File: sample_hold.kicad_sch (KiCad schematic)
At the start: 40 parts, among them K21 G6K-2FY, 5V, Q201 AO3400A, Q202 AO3401A, Q203 AO3400A, Q204 AO3400A, Q205 AO3400A, Q206 AO3400A, Q207 AO3400A, U19 TCA0372, U21 OPA828DGN, U22 OPA2197D

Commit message: Progress checkin.  About to redo FDA feedback again.
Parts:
- removed U19: TCA0372, Package_SO:SOIC-16W_7.5x10.3mm_P1.27mm, symbol Parts:TCA0372
- added C203, C205: 10u, Capacitor_SMD:C_0805_2012Metric, symbol Device:C
- added C210: 0u1, Capacitor_SMD:C_0402_1005Metric, symbol Device:C
- added unit 2 of K21
- added unit 3 of K21
- added R266: 200k, Resistor_SMD:R_0402_1005Metric, symbol Device:R
- added U23: TLV9352D, Parts:TLV9352D, symbol Parts:TLV9352D
- C201: footprint Parts:C_Rect_L31.5mm_W15.0mm_P27.50mm_MKS4 -> Parts:C_Rect_L31.5mm_W15.0mm_P27.50mm_Duo
- C204: value 10n -> 0u1; footprint Capacitor_SMD:C_0603_1608Metric -> Capacitor_SMD:C_0402_1005Metric; LCSC C307500 -> C307331
- K21: footprint Relay_SMD:Relay_DPDT_Omron_G6K-2G-Y -> Relay_SMD:Relay_DPDT_Omron_G6K-2F-Y; symbol Relay:G6K-2 -> Parts:G6K_Split
- R202: value 100k -> 200k; LCSC C25741 -> (none)
- R214: footprint Resistor_SMD:R_0402_1005Metric -> Resistor_SMD:R_0603_1608Metric; LCSC C25087 -> (none)
- U21: footprint Parts:VSSOP-8-1EP_3x3mm_P0.65mm_EP1.57x1.89mm -> Parts:OPA828DGN_guard
- renumbered C205 to C21, Q201 to Q21, Q202 to Q22, Q203 to Q23, Q205 to Q24, Q204 to Q25, Q206 to Q26, Q207 to Q27
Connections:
- net -18V: now also C205.2, C210.2, U23.4 (V-); no longer C207.2, C209.2, U21.4 (V-), U22.4 (V-)
- net DACref: now also U22.5 (+); no longer U22.3 (+)
- net Drive: now also K21.2, K21.3, K21.4, K21.6; no longer K21.3, K21.6
- net GND: now also Q27.3 (D), U22.3 (+); no longer C204.2, Q27.2 (S), U22.5 (+)
- net GNDPWR: now also C204.2, C203.2, C205.1, C210.1
- net SH: now also K21.5; no longer K21.4, K21.5
- net SHGnd: no longer C204.1
- net at R201.1, R202.2: now also C202.2, U22.6 (-), R266.2; no longer C202.1, U22.2 (-)
- net at R202.1, R205.1, R206.1: now also U23.6 (-), U23.7; no longer R203.1, R204.1
- net GComp: now reaches R213.2, R214.1
- net GComp: now also U22.1; no longer U22.7
- net at JP1.2 (B), Q26.3 (D): now also Q27.2 (S); no longer Q27.3 (D)
- net at R212.2, R213.1: now also U22.2 (-); no longer U22.6 (-)
- new net: R203.1, R204.1, R266.1, U23.1, U23.2 (-)
- new net: K21.7, R207.2
- new net +21V: C203.1, C204.1, U23.8 (V+)
- new net -16V: C207.2, C209.2, U21.4 (V-), U22.4 (V-)
- new net DACinner: C202.1, U22.7, U23.3 (+), U23.5 (+)
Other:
- moved on the sheet: C201, C202, C206, C207, C208, C209, C21, D22, JP1, Q24, Q25, Q26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

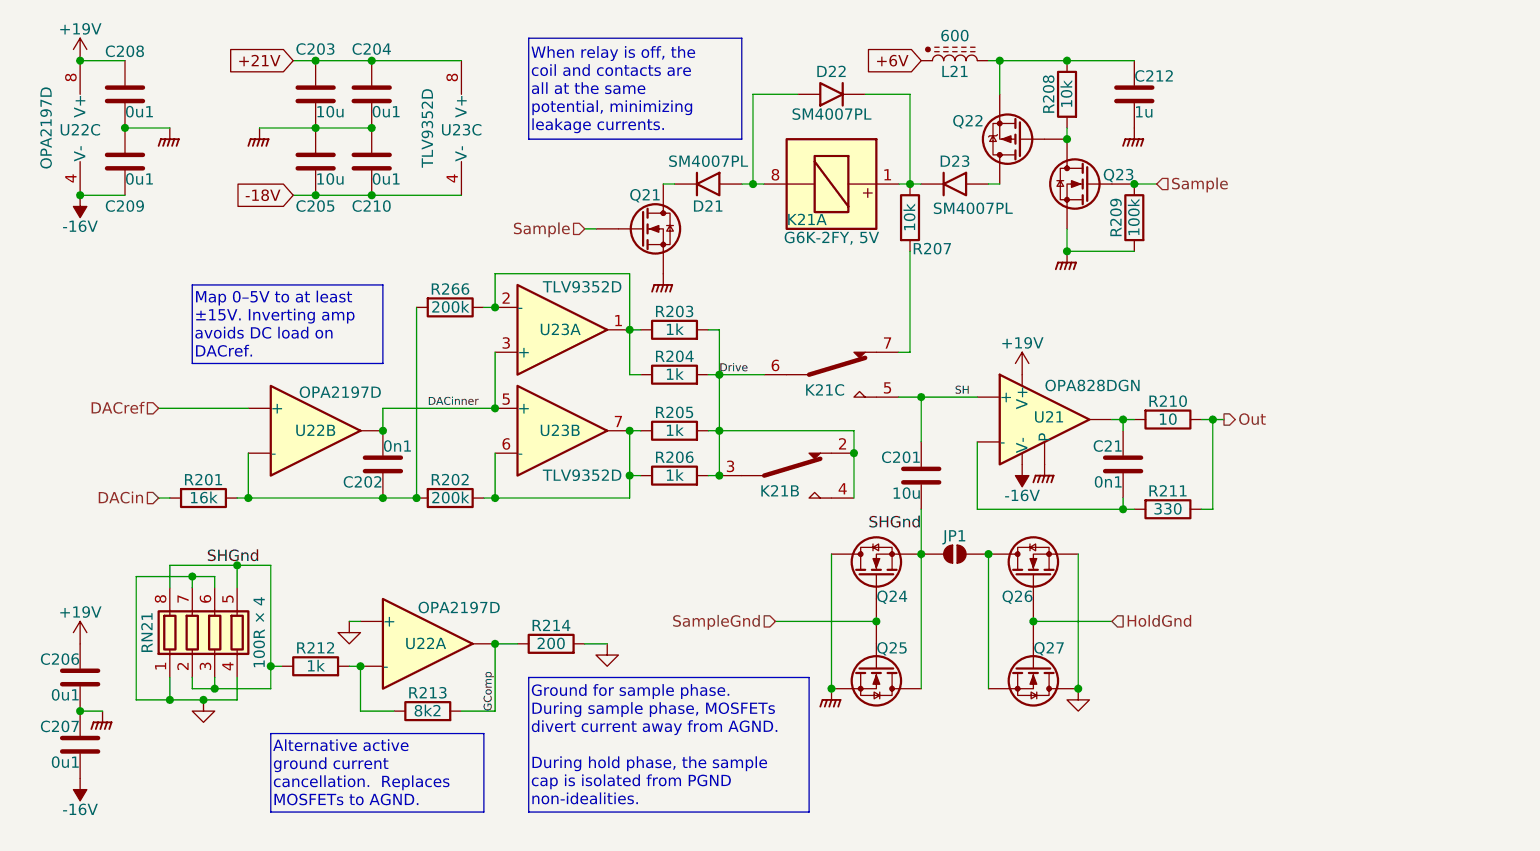
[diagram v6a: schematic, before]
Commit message: Start to place within physical board size.
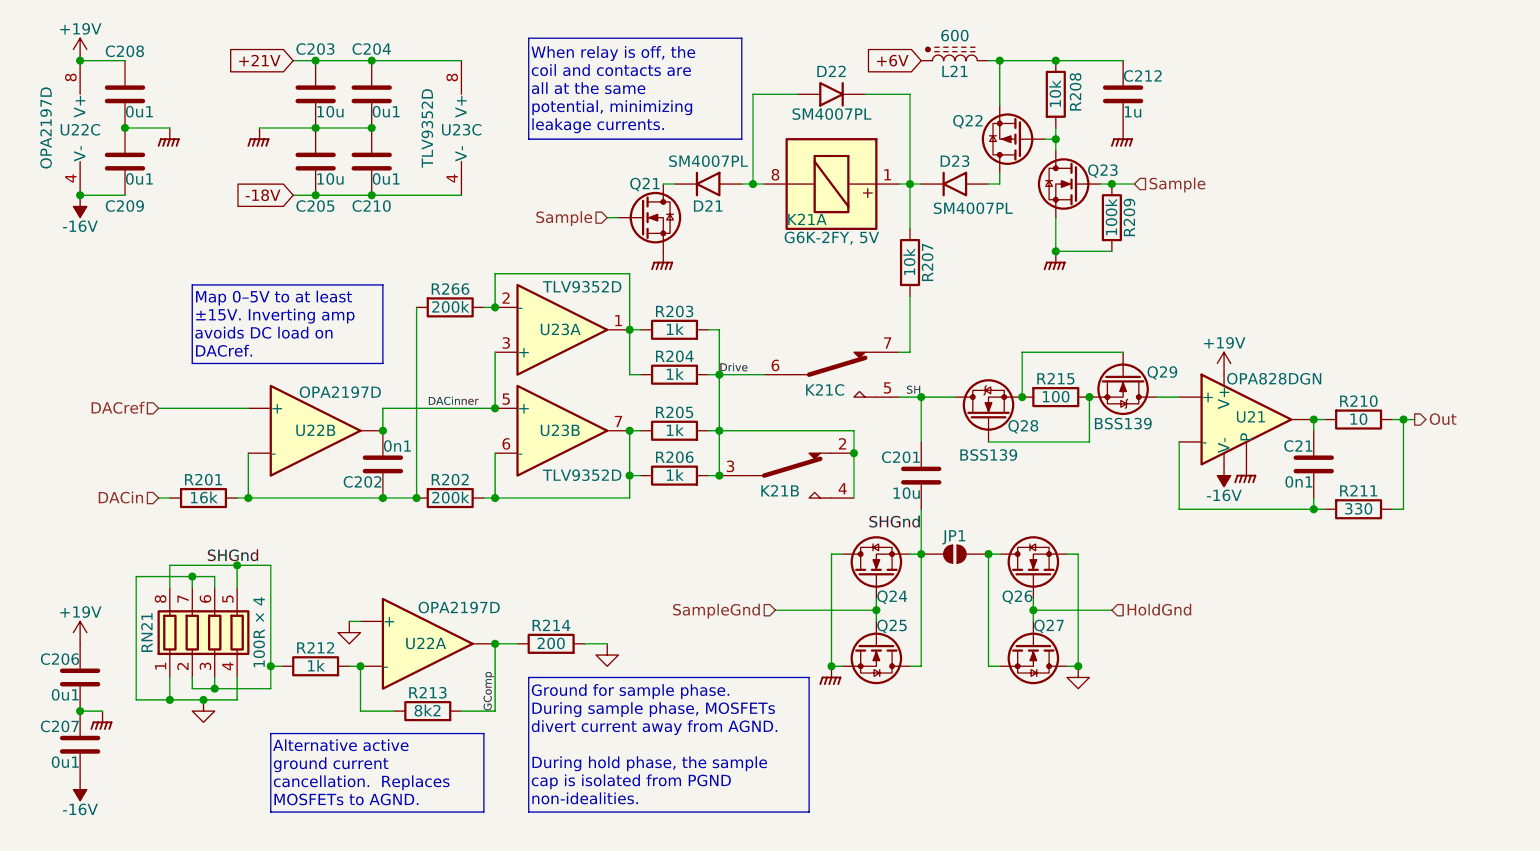
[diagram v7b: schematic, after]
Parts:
- added Q28, Q29: BSS139, Parts:SOT-23, symbol Parts:BSS139
- added R215: 100, Resistor_SMD:R_0402_1005Metric, symbol Device:R
- Q21, Q23, Q24, Q25, Q26, Q27: symbol Transistor_FET:AO3400A -> Parts:AO3400A; LCSC C20917 -> C15127
- Q22: symbol Transistor_FET:AO3401A -> Parts:AO3401A
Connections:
- net SH: now also Q28.3 (D); no longer U21.3 (+)
- new net: Q28.1 (G), Q29.2 (S), R215.1
- new net: Q28.2 (S), Q29.1 (G), R215.2
- new net: Q29.3 (D), U21.3 (+)
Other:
- moved on the sheet: C21, C212, Q21, Q22, Q23, Q24, Q25, Q26, Q27, R207, R208, R209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

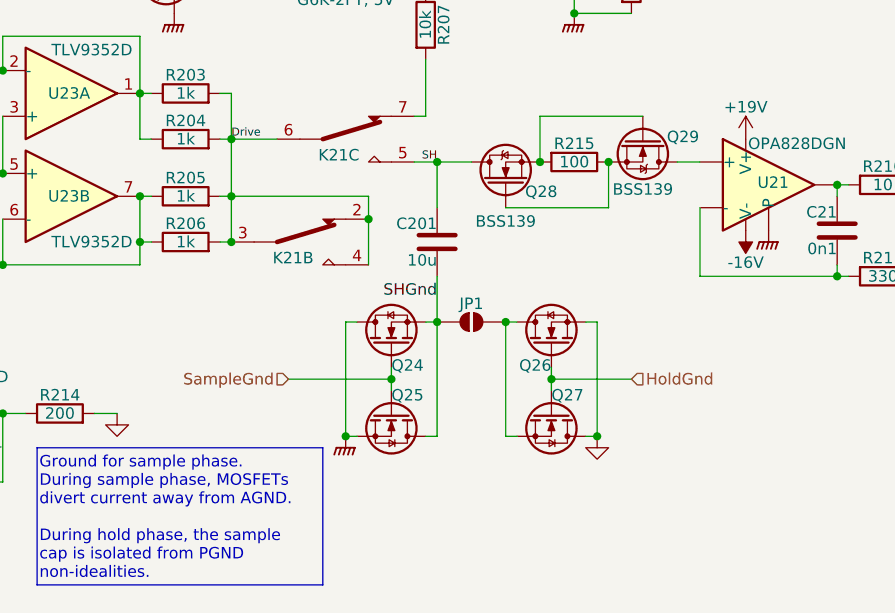
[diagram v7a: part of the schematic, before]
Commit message: Power mostly routed
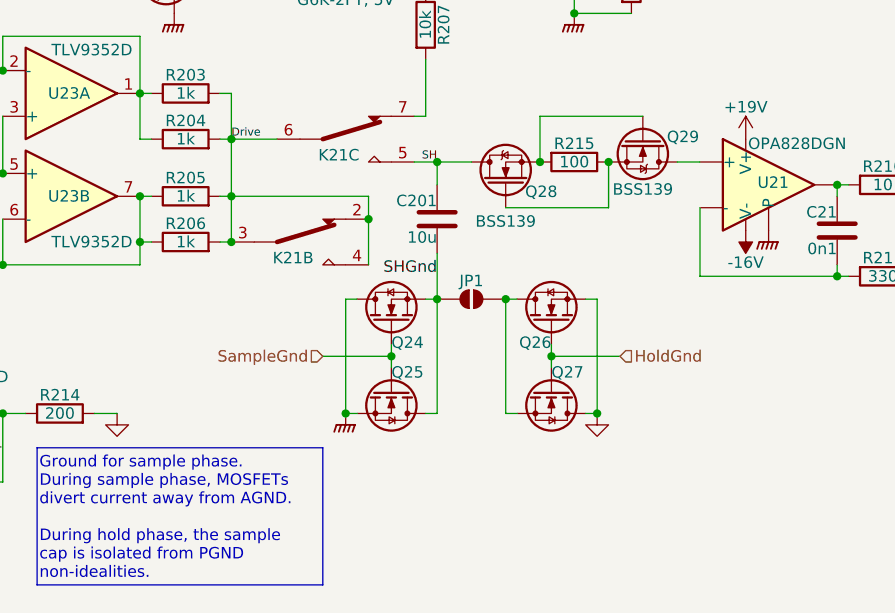
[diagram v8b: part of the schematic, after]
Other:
- moved on the sheet: C201, JP1, Q24, Q25, Q26, Q27
